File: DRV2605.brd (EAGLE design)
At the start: 49.9 x 35 mm, 107 parts, among them J1 BM06B-SRSS-TB, J2 BM06B-SRSS-TB, J3 BM06B-SRSS-TB, J4 BM06B-SRSS-TB, J5 BM06B-SRSS-TB, J6 JST_6_PIN_VERTICAL, U1 DRV2605L, U11 NRF51X22_QFQF, U2 DRV2605L, U3 DRV2605L, U4 DRV2605L, U5 DRV2605L, U6 DRV2605L, U7 BNO080, U8 TCA9548APWR, U9 TCA9548APWR, X1 32.768kHz, X2 8MHz, X4 16MHz, X5 32.768kHz, Y1 32.768kHz

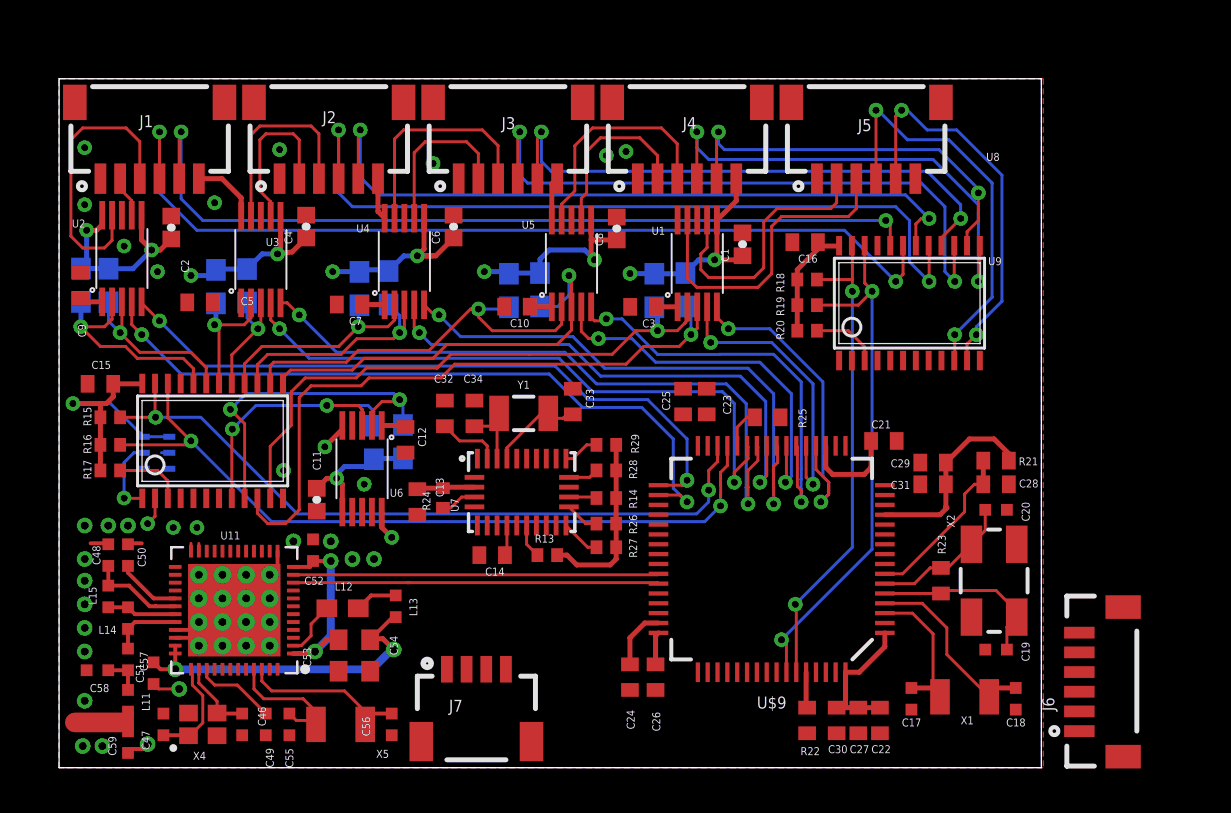
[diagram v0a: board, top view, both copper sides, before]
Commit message: 6DRVs ARM IMU on board - done; palmIMU/battery/programming connector
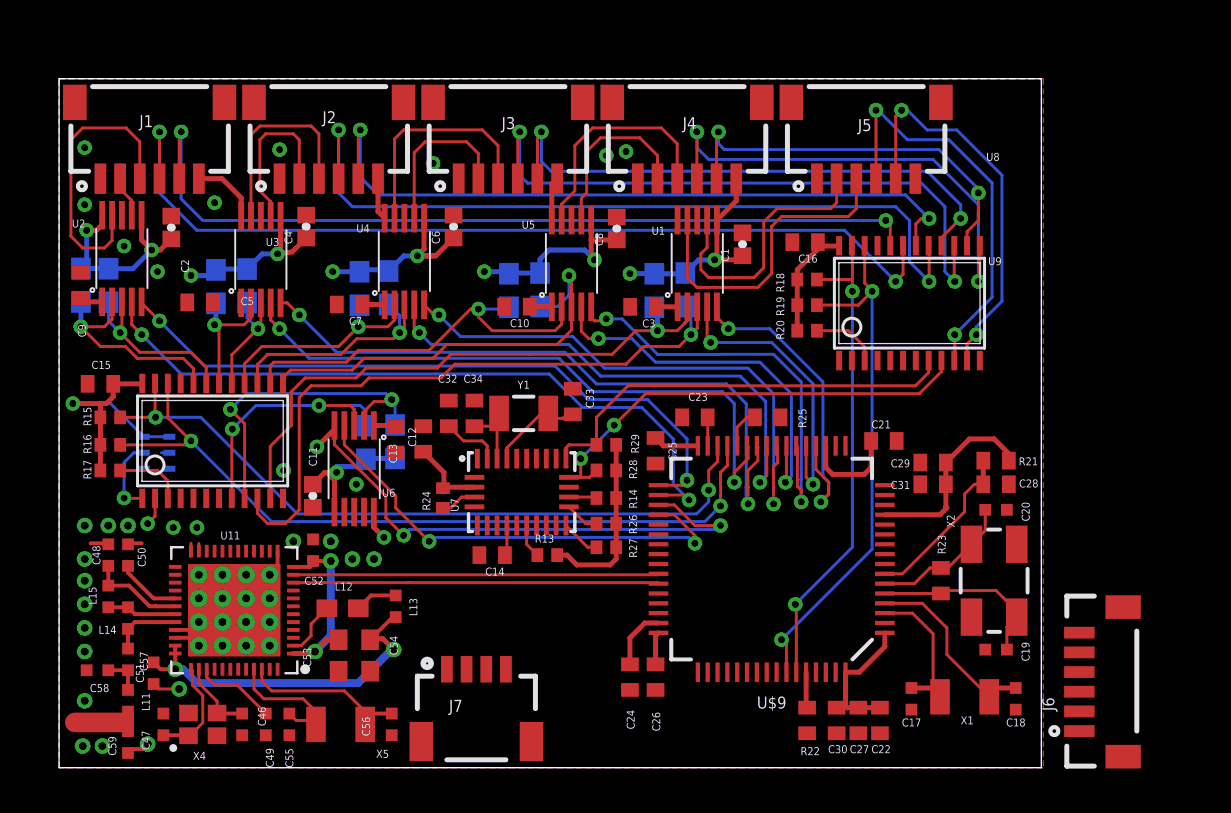
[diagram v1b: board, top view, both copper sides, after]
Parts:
- moved C13 3.21 mm to (18.5, 16.7), turned to 90 degrees
- moved C25 2.87 mm to (30.3, 16.1), turned to 270 degrees
- moved C23 1.00 mm to (32.3, 17.8), turned to 180 degrees
- moved C12 0.50 mm to (17.1, 16.7)
- moved R12 0.40 mm to (15.6, 16.5)
- moved U6 0.40 mm to (14.9, 15.5)
- moved R11 0.40 mm to (17.1, 16.6)
- moved C11 0.28 mm to (12.9, 13.8)
- moved C32 0.20 mm to (19.8, 18.0)
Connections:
- removed net PS0/WAKE: U7.6
- removed net PS1: U7.5
- removed net SCL/SCK/RX: R28.1, U7.19
- removed net SDA/MISO/TX: R29.1, U7.20
- net EN6: now also U$9.35
- net GND: now also U7.5, U7.6
- net IMU_SCL6: now also R28.1, U7.19
- net IMU_SDA6: now also R29.1, U7.20
- net IN/TRIG6: now also U$9.36
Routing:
- net EN6: track 1.45 -> 28.4 mm, vias 1 -> 3
- net IN/TRIG6: track 0.00 -> 24.1 mm, vias 0 -> 2
- net IMU_SCL6: track 0.00 -> 23.2 mm, vias 0 -> 2
- net IMU_SDA6: track 0.00 -> 22.0 mm
- net VCC: track 112.2 -> 115.1 mm
- net SDA/MISO/TX: track 1.84 -> 0.00 mm
- net SCL/SCK/RX: track 1.54 -> 0.00 mm
- net N$5: track 0.00 -> 1.45 mm
- net 3.3V: track 15.3 -> 16.0 mm
- net AVDD: track 17.1 -> 17.7 mm

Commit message: glove connector;programming pins;NRF antenna left
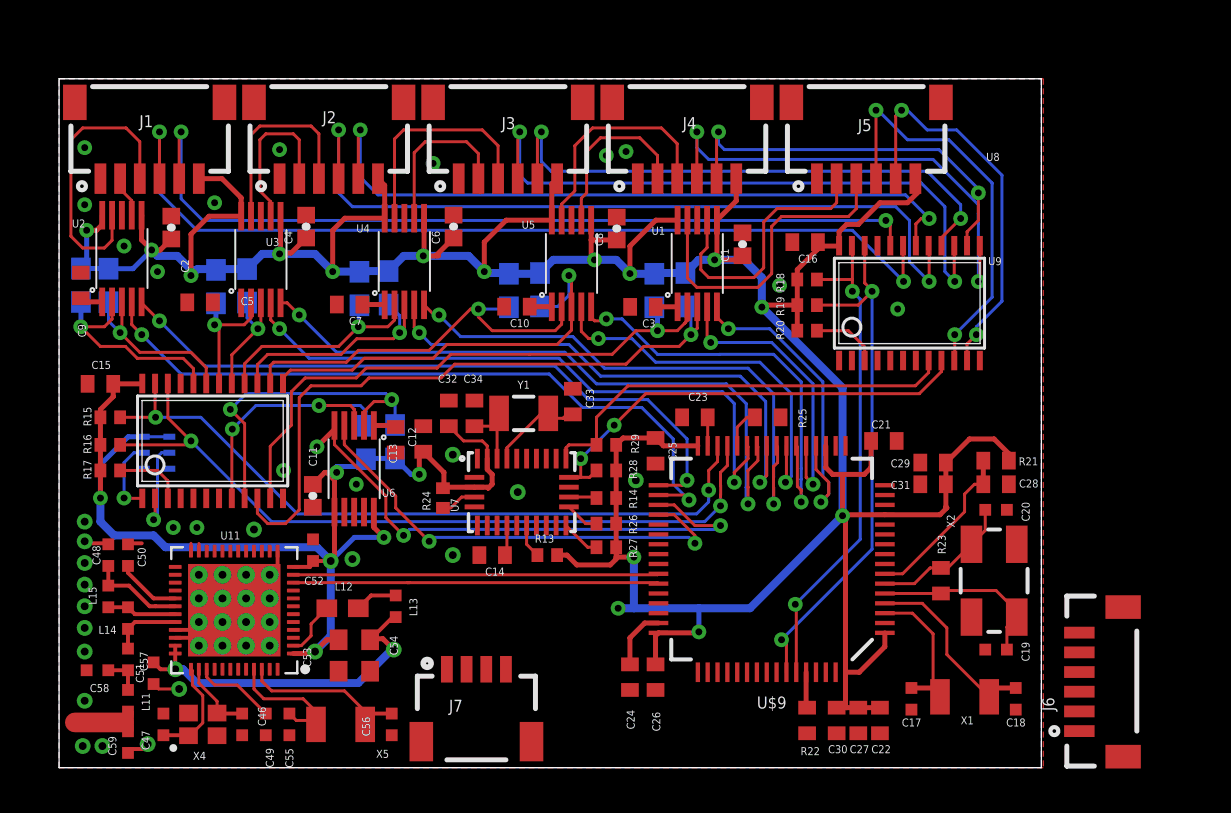
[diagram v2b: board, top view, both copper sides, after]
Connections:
- removed net 3.3V: C13.1, C32.1, R13.2, R14.2, R24.2, R26.2, R27.2, R28.2, R29.2, U7.28, U7.3
- removed net VDD_NRF: C52.1, C53.1, U11.1, U11.12
- net VCC: now also C13.1, C32.1, C52.1, C53.1, R13.2, R14.2, R24.2, R26.2, R27.2, R28.2, R29.2, U11.1, U11.12, U7.28, U7.3
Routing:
- net VCC: track 115.1 -> 253.5 mm, vias 13 -> 21
- net 3.3V: track 16.0 -> 0.00 mm
- net VDD_NRF: track 9.93 -> 0.04 mm, vias 2 -> 0
- net N$30: track 1.84 -> 5.08 mm
- net GND: vias 28 -> 31

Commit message: glove connector;programming pins;NRF antenna
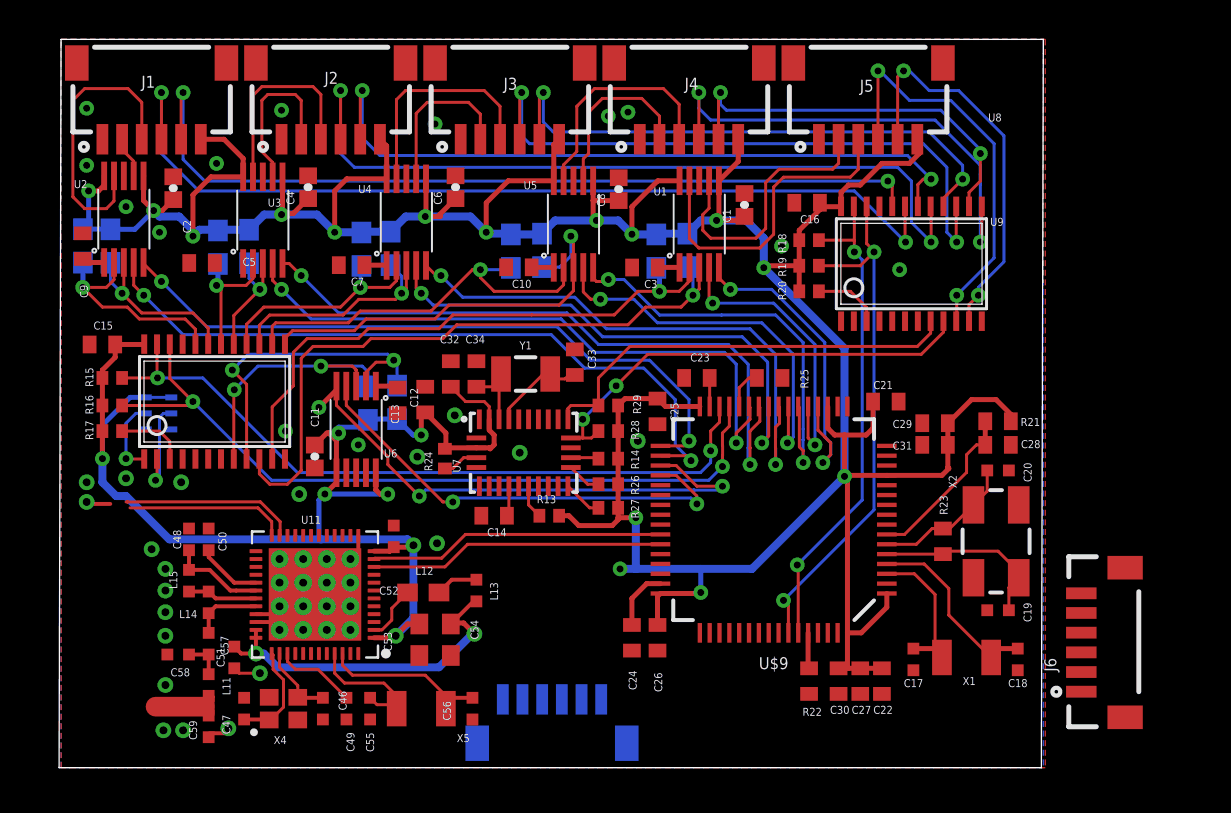
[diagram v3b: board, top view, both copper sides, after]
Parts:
- J7: value (none) -> JST_6_PIN_VERTICAL; device SparkFun-Connectors:1X04_1MM_RA -> SparkFun-Connectors:JST-6-SMD-VERT-1.0MM
- moved J7 4.72 mm to (25.0, 2.20), flipped to the bottom
- moved C53 4.18 mm to (18.3, 6.50)
- moved C55 4.18 mm to (15.8, 3.00)
- moved C56 4.18 mm to (21.0, 3.00)
- moved C47 4.18 mm to (9.40, 3.00)
- moved C51 4.18 mm to (8.90, 5.60)
- moved L12 4.18 mm to (18.5, 8.90)
- moved L14 4.18 mm to (7.60, 8.40)
- moved L15 4.18 mm to (6.60, 9.50)
- moved U11 4.18 mm to (13.0, 8.80)
- moved X4 4.18 mm to (11.4, 3.00)
- moved C46 4.18 mm to (13.4, 3.00)
- moved C48 4.18 mm to (6.60, 11.6)
- moved C49 4.18 mm to (14.6, 3.00)
- moved C50 4.18 mm to (7.60, 11.6)
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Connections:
- new net N$15: J7.1
- new net N$17: J7.2
- new net N$18: J7.3
- new net N$20: J7.4
- new net N$21: J7.5
- new net N$22: J7.6
- net +OUT6: no longer J7.3
- net -OUT6: no longer J7.4
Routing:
- net SWDIO/NRESET: track 0.39 -> 8.96 mm, vias 1 -> 0
- net SWDCLK: track 0.40 -> 8.19 mm, vias 1 -> 0
- net VCC: track 253.5 -> 259.5 mm, vias 21 -> 22
- net BLE_TX: track 18.7 -> 15.0 mm
- net BLE_RX: track 18.6 -> 15.1 mm
- net GND: track 24.3 -> 23.6 mm, vias 31 -> 33
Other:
- board size 49.9 x 35 mm -> 50 x 37 mm

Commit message: NRF antenna yet to be done; glove 50mm wide
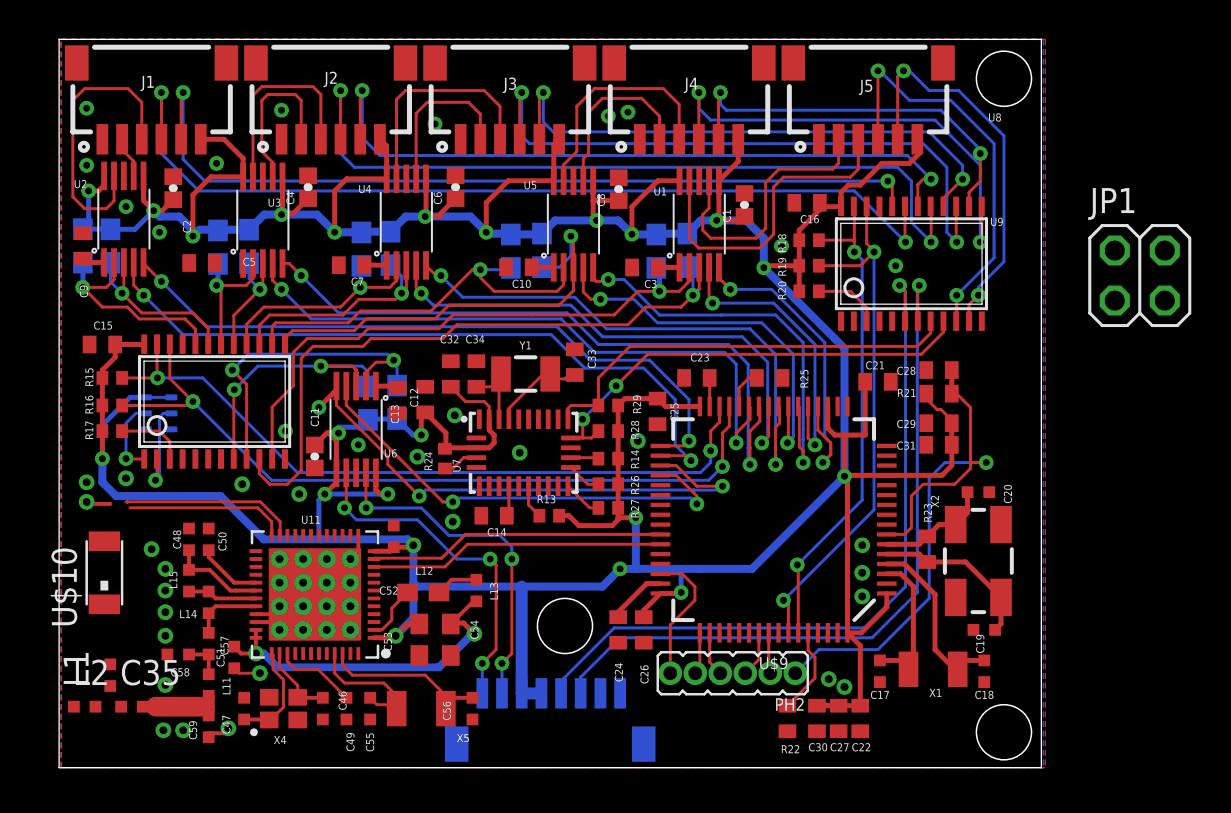
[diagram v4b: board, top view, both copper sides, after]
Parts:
- removed J6, J7: JST_6_PIN_VERTICAL, SparkFun-Connectors:JST-6-SMD-VERT-1.0MM
- added C35: 1.0pF, Nordic_nRF:RESC0402_N
- added JP1: (no value), pinhead:2X02
- added L1: 2.7nH, Nordic_nRF:RESC0402_N
- added L2: 3.9nH, Nordic_nRF:RESC0402_N
- added PH2: PH1X6-05, pel_hdr:PH005-1-6
- added U$10: ANT_2450AT18B100E, Johanson_antennas:2450AT18B100E
- added U$11: JST_SR/SZ_8POS_VERTICAL, yhtomit_connectors:JST_SR/SZ_VERTICAL_8POS
- moved C28 4.84 mm to (44.7, 20.2), turned to 180 degrees
- moved R21 3.31 mm to (44.7, 19.0), turned to 0 degrees
- moved C27 2.20 mm to (39.6, 2.50)
- moved C30 2.20 mm to (38.5, 2.50)
- moved R22 2.20 mm to (37.0, 2.50)
- moved C22 2.20 mm to (40.7, 2.50)
- moved C18 1.80 mm to (47.0, 4.90)
- moved X1 1.80 mm to (44.4, 5.00)
- moved C17 1.80 mm to (41.7, 4.90)
- moved C20 1.49 mm to (46.7, 14.0)
- moved X2 1.35 mm to (46.7, 10.5)
- moved C19 1.22 mm to (47.0, 7.00)
- moved C21 1.08 mm to (41.6, 19.6)
- moved R23 0.89 mm to (44.1, 11.1)
- moved C24 0.81 mm to (28.4, 7.00)
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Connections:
- removed net 1SCL1: U9.7
- removed net 1SDA1: U9.6
- removed net N$18: J7.3
- removed net N$20: J7.4
- removed net N$21: J7.5
- removed net N$22: J7.6
- new net EM_RX: JP1.3, U$9.16
- new net EM_TX: JP1.1, U$9.17
- new net IMU_SCL7: U$11.6, U9.7
- new net IMU_SDA7: U$11.5, U9.6
- net +OUT6: now also U$11.1
- net -OUT6: now also U$11.2
- net GND: now also JP1.4, L1.1, U$11.7, U$11.8
- net N$15: now also C35.1, L1.2, L2.2; no longer J7.1
- net N$17: now also L2.1, U$10.P$1; no longer J7.2
- net RF: now also C35.2
- net RST: now also PH2.1; no longer J6.6
- net TCK: now also PH2.5; no longer J6.4
- net TDI: now also PH2.4; no longer J6.3
- net TDO: now also PH2.3; no longer J6.2
- net TMS: now also PH2.6; no longer J6.5
- net TRST: now also PH2.2; no longer J6.1
- net VCC: now also JP1.2, U$11.3, U$11.4
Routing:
- net IMU_SDA7: track 0.00 -> 37.5 mm, vias 0 -> 1
- net IMU_SCL7: track 0.00 -> 37.2 mm, vias 0 -> 1
- net RST: track 8.68 -> 30.6 mm, vias 0 -> 1
- net -OUT6: track 0.00 -> 17.6 mm, vias 0 -> 3
- net +OUT6: track 0.00 -> 17.5 mm, vias 0 -> 3
- net VCC: track 259.5 -> 276.4 mm
- net TMS: track 0.00 -> 6.94 mm
- net N$3: track 1.82 -> 4.50 mm
- net TDO: track 0.00 -> 2.34 mm
- net TDI: track 0.00 -> 2.28 mm
- net TCK: track 0.00 -> 2.15 mm
- net TRST: track 0.00 -> 2.08 mm
- net PH1: track 7.34 -> 5.81 mm
- net PH0: track 9.35 -> 8.49 mm
- net GND: vias 33 -> 38
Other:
- board size 50 x 37 mm -> 49.9 x 37 mm

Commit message: board done awaiting validation
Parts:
- removed JP1: (no value), pinhead:2X02
- removed U$11: JST_SR/SZ_8POS_VERTICAL, yhtomit_connectors:JST_SR/SZ_VERTICAL_8POS
- added C36, C37: 0.1uf, rcl:C0402
- added J6: (no value), SparkFun-Connectors:1X04
- added PH1: PH1X4-05, pel_hdr:PH005-1-4
- added U$12: TTP223_SOT23-6, yhtomit_ICs:SOT23-6
- added U$13: JST_SR/SZ_9POS_VERTICAL, yhtomit_connectors:JST_SR/SZ_VERTICA_9POS
- X2: device SparkFun-Clocks:CRYSTAL-SMD-5X3.2-4PAD -> yhtomit_XTAL:CRYSTAL-SMD-5X3.2-4PAD
- moved C28 6.86 mm to (50.6, 16.7)
- moved R21 6.81 mm to (50.6, 15.6)
- moved C15 3.50 mm to (5.70, 21.5)
- moved L2 3.49 mm to (2.10, 6.50), turned to 270 degrees
- moved J2 3.30 mm to (17.1, 36.7)
- moved J3 3.30 mm to (26.2, 36.7)
- moved J1 3.30 mm to (8.00, 36.7)
- moved J4 3.30 mm to (35.3, 36.7)
- moved J5 3.30 mm to (44.4, 36.7)
- moved C23 3.10 mm to (35.5, 19.8)
- moved C21 3.08 mm to (44.6, 18.9)
- moved C17 3.01 mm to (44.7, 5.10)
- moved C26 3.00 mm to (32.7, 7.00)
- moved R1 3.00 mm to (33.3, 26.2)
- moved C49 3.00 mm to (17.6, 3.00)
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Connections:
- new net IN: C37.1, U$12.3, U$13.5
- new net N$22: U$12.6
- new net N$24: U$12.4
- new net Q: U$12.1, U$9.45
- net +OUT6: now also U$13.1; no longer U$11.1
- net -OUT6: now also U$13.2; no longer U$11.2
- net EM_RX: now also J6.3; no longer JP1.3
- net EM_TX: now also J6.2; no longer JP1.1
- net GND: now also C36.2, C37.2, J6.4, PH1.1, U$12.2, U$13.8, U$13.9, X2.2, X2.4; no longer JP1.4, U$11.7, U$11.8
- net IMU_SCL7: now also U$13.7; no longer U$11.6
- net IMU_SDA7: now also U$13.6; no longer U$11.5
- net SWDCLK: now also PH1.3
- net SWDIO/NRESET: now also PH1.2
- net VCC: now also C36.1, J6.1, PH1.4, U$12.5, U$13.3, U$13.4; no longer JP1.2, U$11.3, U$11.4
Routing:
- net VCC: track 276.4 -> 296.5 mm
- net EM_TX: track 0.00 -> 15.7 mm
- net SWDIO/NRESET: track 8.96 -> 23.0 mm
- net SWDCLK: track 8.19 -> 21.5 mm
- net EM_RX: track 0.00 -> 13.1 mm
- net IN: track 0.00 -> 8.58 mm, vias 0 -> 2
- net RST: track 30.6 -> 24.6 mm
- net RF: track 4.70 -> 10.1 mm
- net Q: track 0.00 -> 5.05 mm
- net IMU_SDA5: track 20.7 -> 17.2 mm
- net IMU_SCL5: track 20.3 -> 17.1 mm
- net N$15: track 0.00 -> 2.14 mm
- net GND: track 23.6 -> 21.6 mm, vias 38 -> 145
- net IMU_SCL3: track 28.7 -> 27.1 mm
- net N$13: track 0.00 -> 1.45 mm
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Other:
- board size 49.9 x 37 mm -> 52.9 x 37 mm
